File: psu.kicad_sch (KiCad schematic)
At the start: 70 parts, among them J6 Screw_Terminal_01x02, J7 Screw_Terminal_01x03, U12 ADP7182AUJZ, U13 ADP7182AUJZ, U14 AZ1117-ADJ, U15 AZ1117-ADJ, U16 AZ1117-ADJ

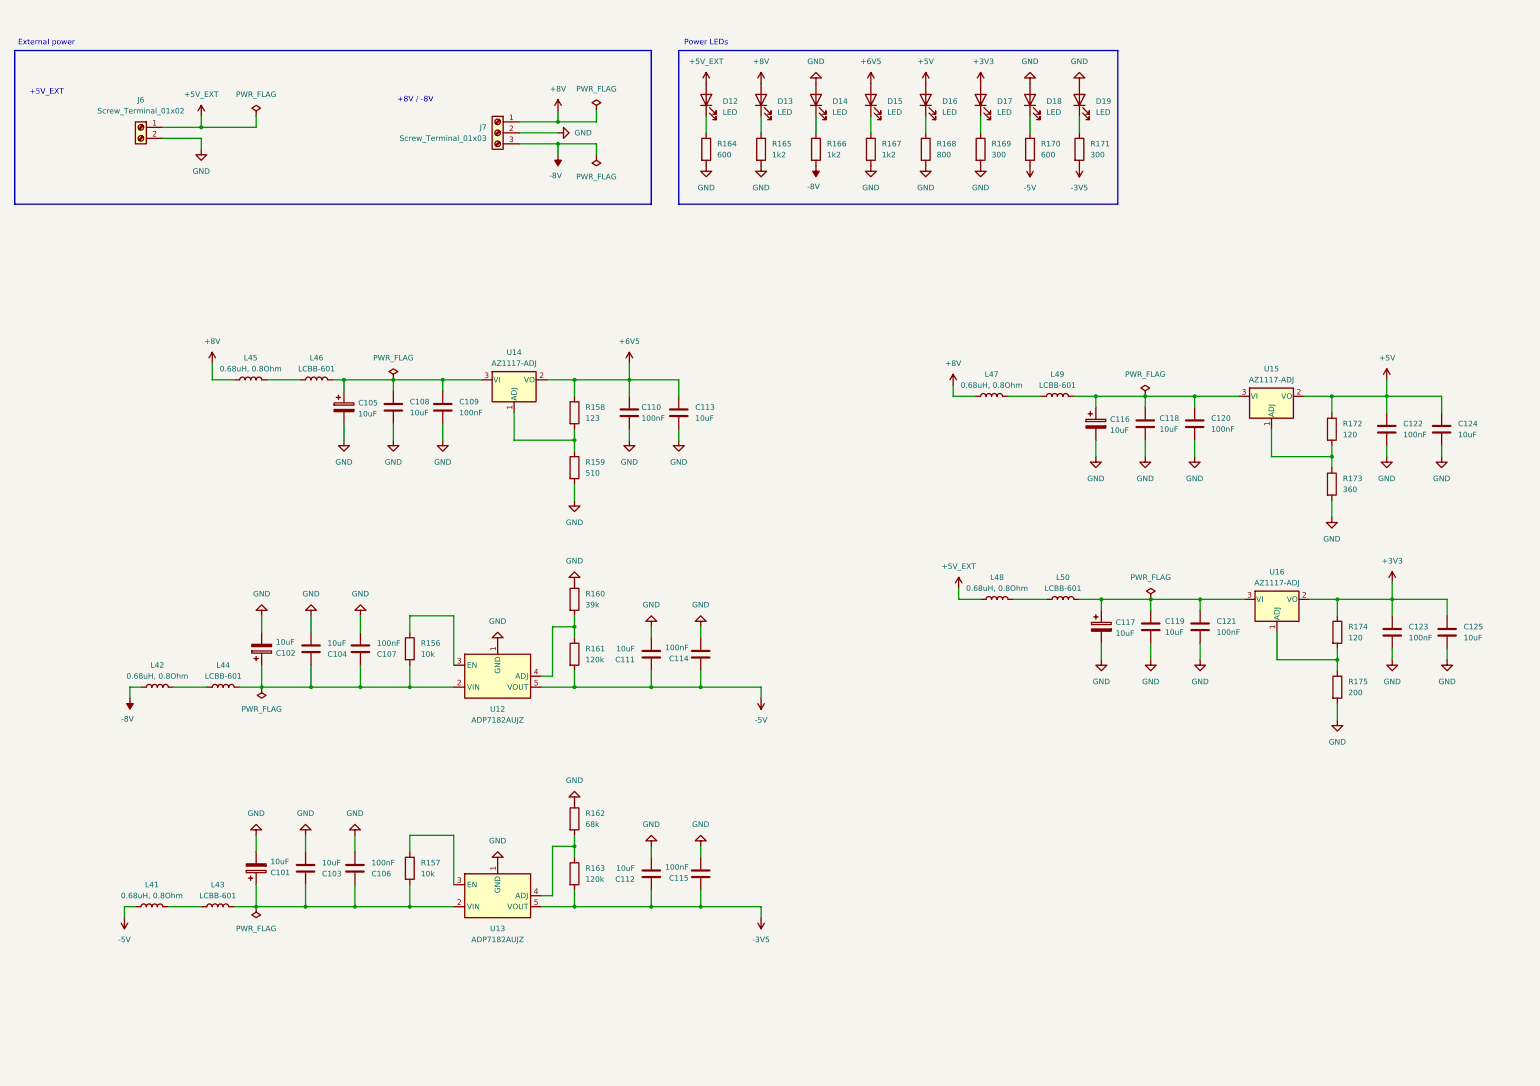
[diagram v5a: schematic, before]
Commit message: Apply changes after review, left to fix: comparator histeresis, PSU missing lines?
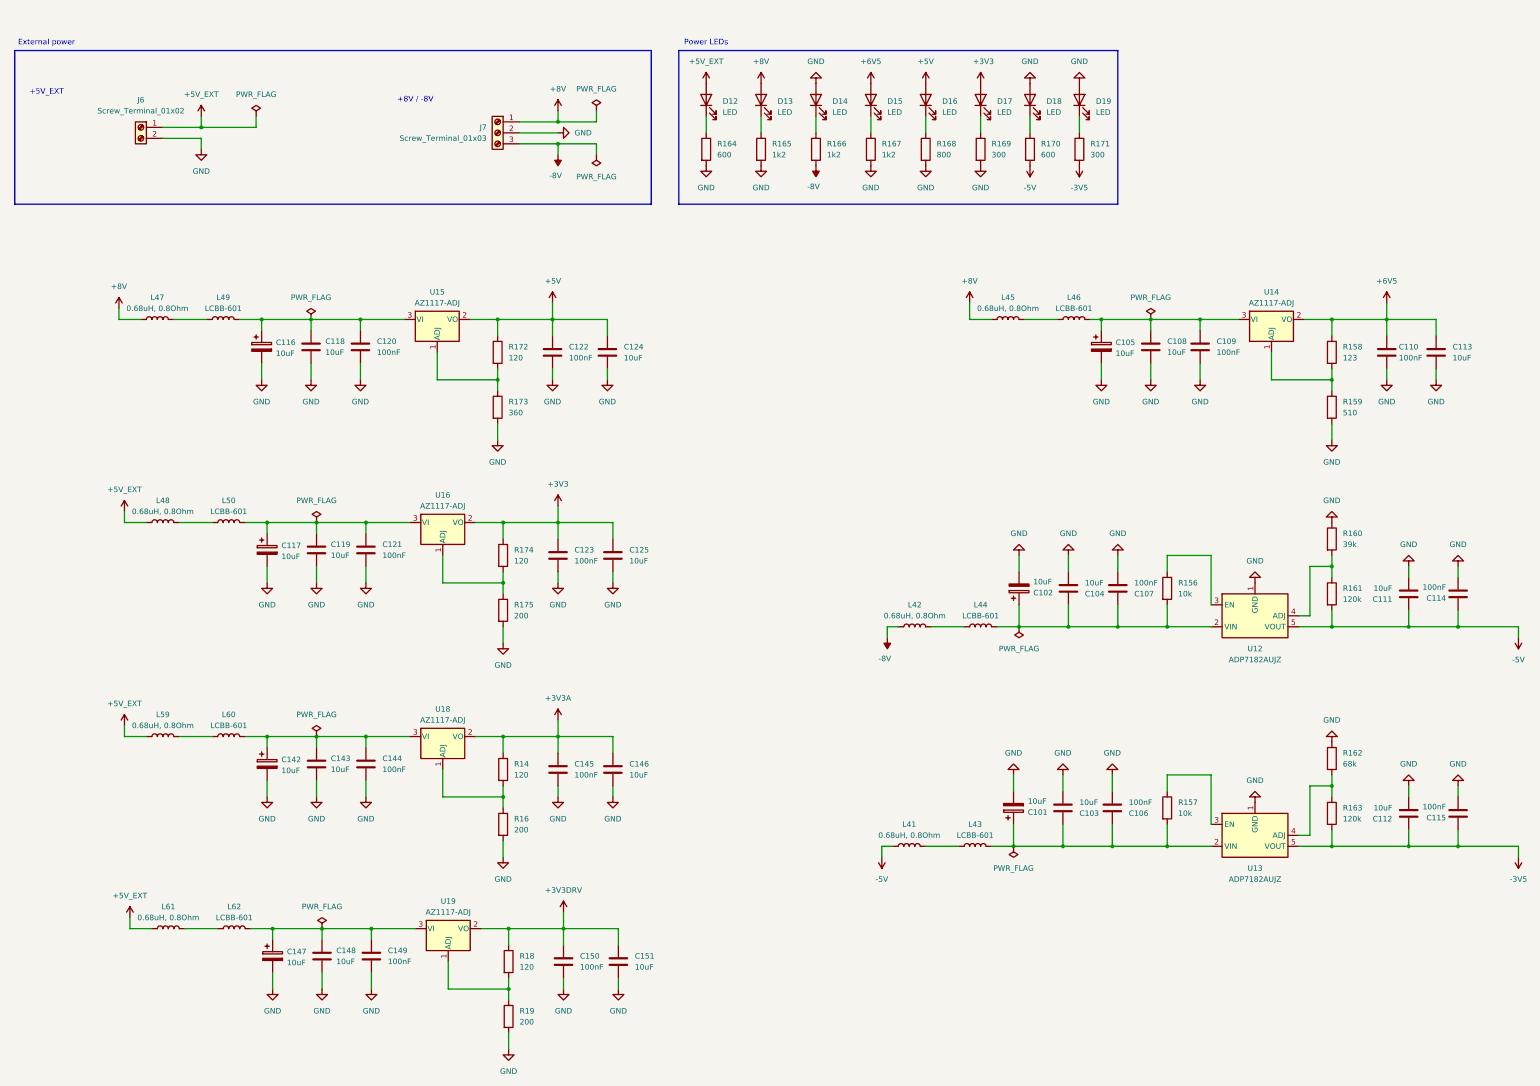
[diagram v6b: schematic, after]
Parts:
- added C142, C147: 10uF, Capacitor_SMD:C_0805_2012Metric, symbol Device:C_Polarized
- added C143, C146, C148, C151: 10uF, Capacitor_SMD:C_0805_2012Metric, symbol Device:C
- added C144, C145, C149, C150: 100nF, Capacitor_SMD:C_0805_2012Metric, symbol Device:C
- added L59, L61: 0.68uH, 0.8Ohm, Inductor_SMD:L_0805_2012Metric, symbol Device:L
- added L60, L62: LCBB-601, Inductor_SMD:L_0805_2012Metric, symbol Device:L
- added R14, R18: 120, Resistor_SMD:R_0805_2012Metric, symbol Device:R
- added R16, R19: 200, Resistor_SMD:R_0805_2012Metric, symbol Device:R
- added U18, U19: AZ1117-ADJ, Package_TO_SOT_SMD:SOT-89-3, symbol Regulator_Linear:AZ1117-ADJ
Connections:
- net +5V_EXT: now also L59.1, L61.1
- net GND: now also C142.2, C143.2, C144.2, C145.2, C146.2, C147.2, C148.2, C149.2, C150.2, C151.2, R16.2, R19.2
- new net: L61.2, L62.1
- new net: C147.1, C148.1, C149.1, L62.2, U19.3 (VI)
- new net: L59.2, L60.1
- new net: R18.2, R19.1, U19.1 (ADJ)
- new net: R14.2, R16.1, U18.1 (ADJ)
- new net: C142.1, C143.1, C144.1, L60.2, U18.3 (VI)
- new net +3V3A: C145.1, C146.1, R14.1, U18.2 (VO)
- new net +3V3DRV: C150.1, C151.1, R18.1, U19.2 (VO)
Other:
- moved on the sheet: C101, C102, C103, C104, C105, C106, C107, C108, C109, C110, C111, C112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

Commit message: Fix footprints and allign components placements
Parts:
- D12, D13, D14: footprint Diode_THT:D_DO-41_SOD81_P10.16mm_Horizontal -> LED_SMD:LED_0805_2012Metric
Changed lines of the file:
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@@
 			)
 		)
-		(property "Footprint" "Diode_THT:D_DO-41_SOD81_P10.16mm_Horizontal"
+		(property "Footprint" "LED_SMD:LED_0805_2012Metric"
 			(at 180.34 36.83 0)
 			(effects
@@
 			)
 		)
-		(property "Footprint" "Diode_THT:D_DO-41_SOD81_P10.16mm_Horizontal"
+		(property "Footprint" "LED_SMD:LED_0805_2012Metric"
 			(at 205.74 36.83 0)
 			(effects
@@
 			)
 		)
-		(property "Footprint" "Diode_THT:D_DO-41_SOD81_P10.16mm_Horizontal"
+		(property "Footprint" "LED_SMD:LED_0805_2012Metric"
 			(at 193.04 36.83 0)
 			(effects

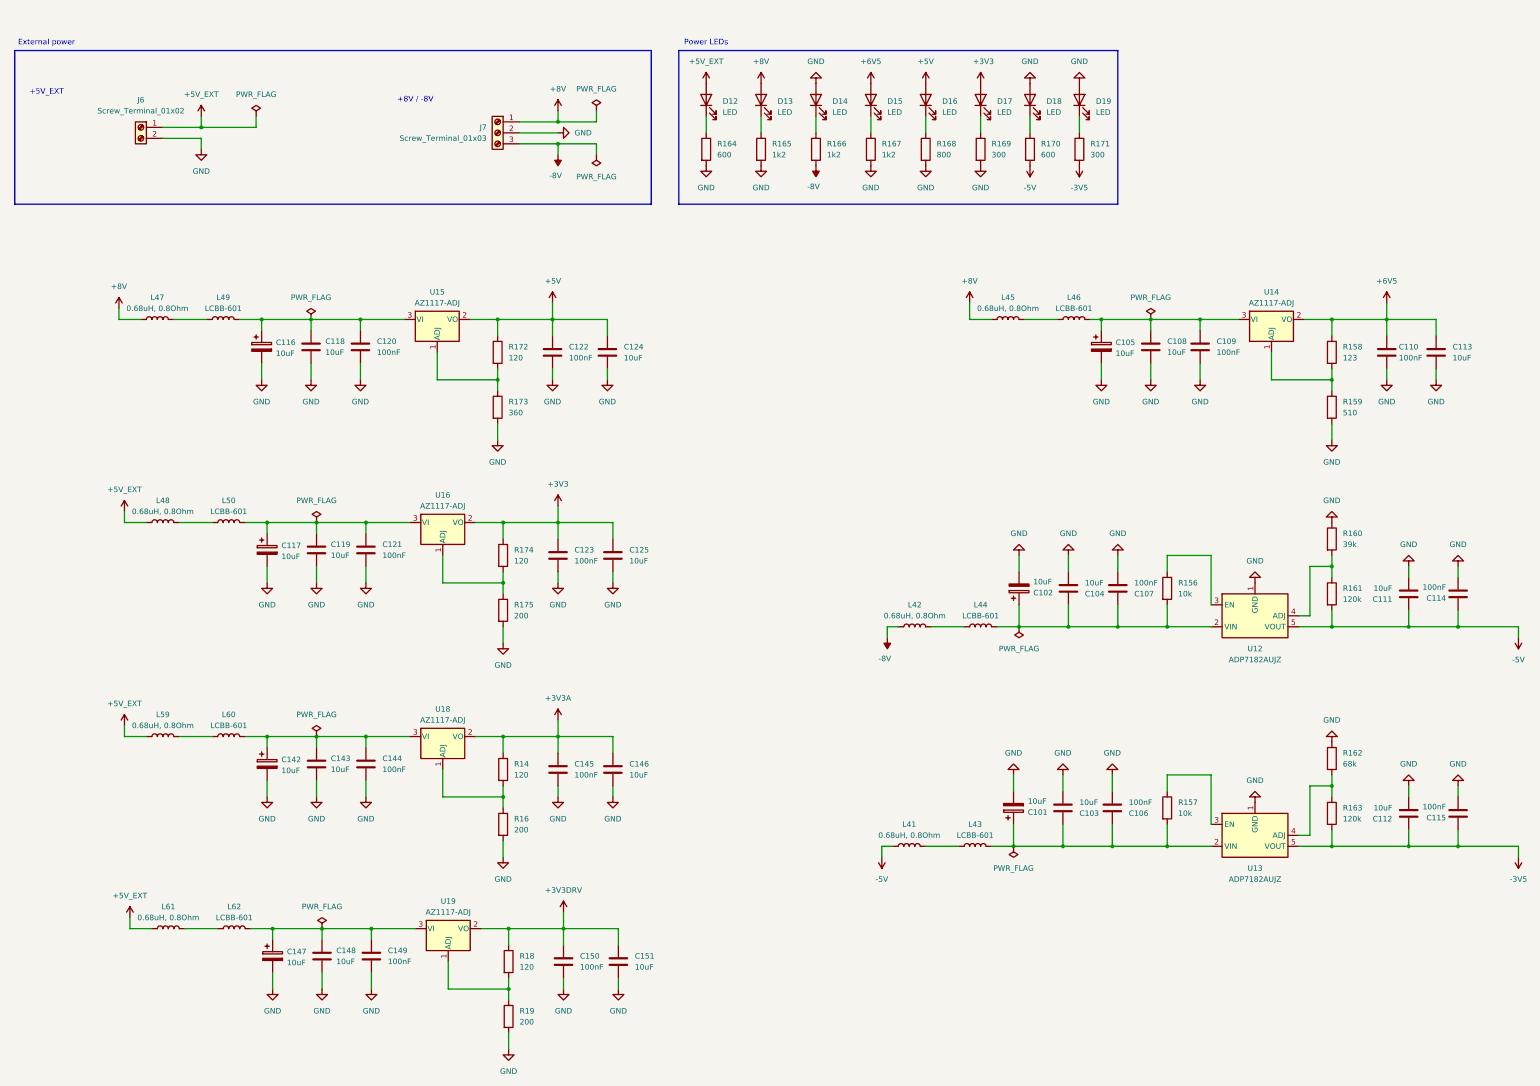
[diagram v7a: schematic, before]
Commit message: Route AFE - attenuators
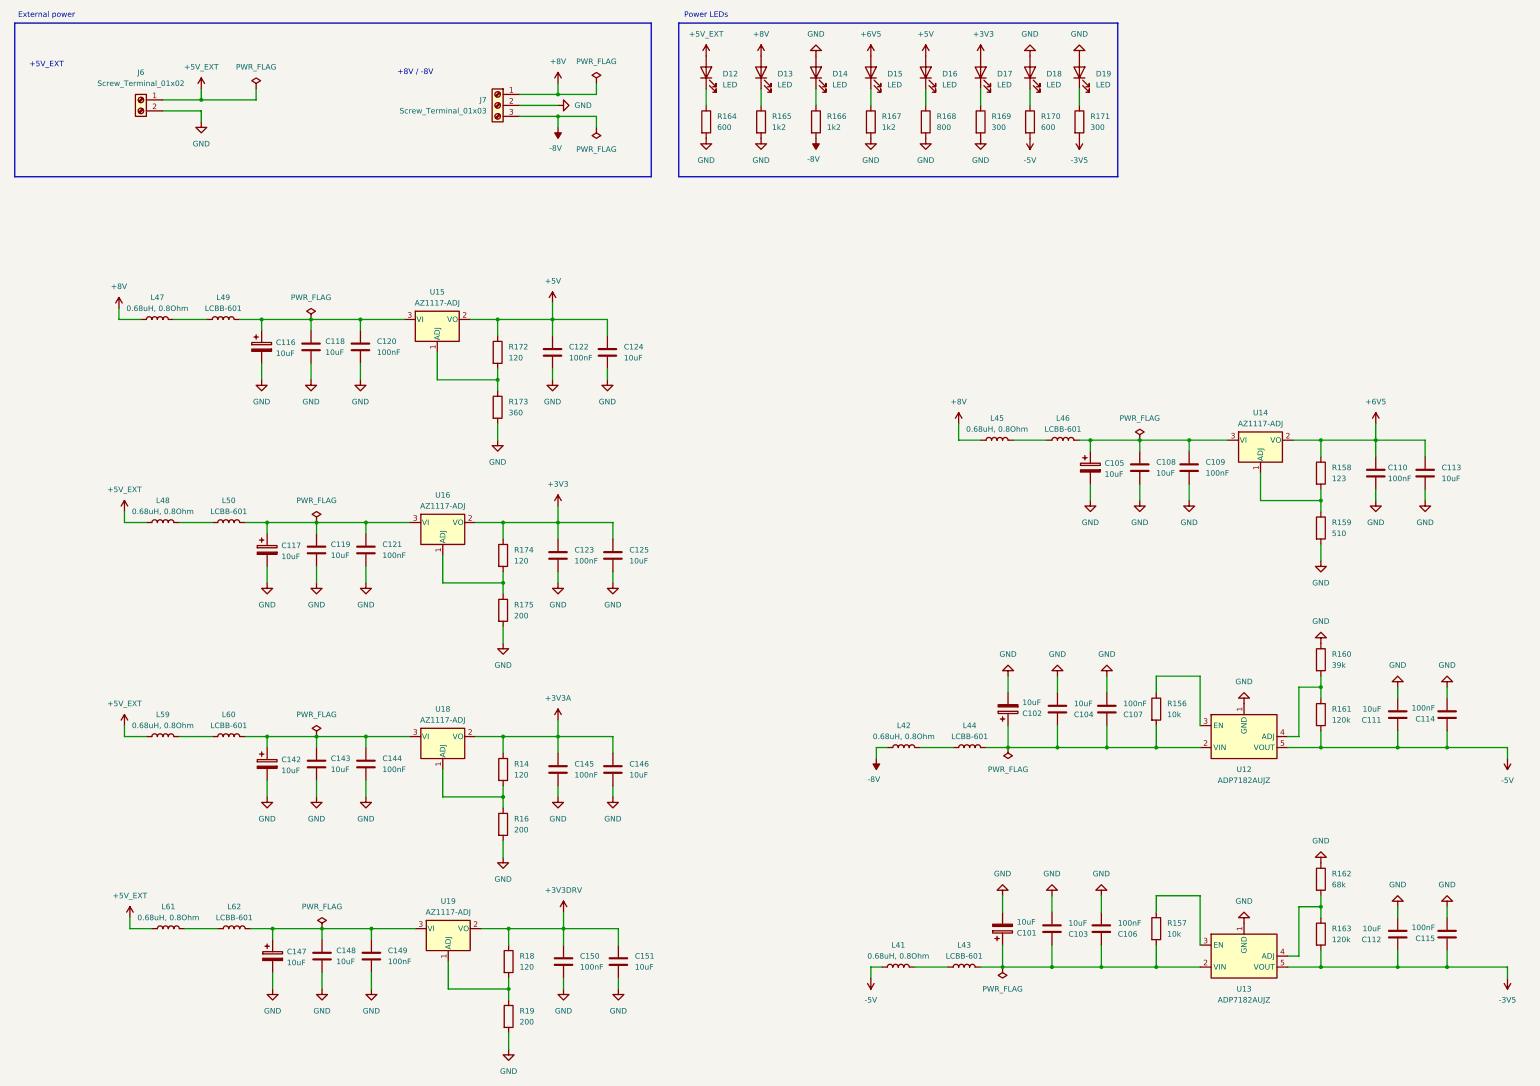
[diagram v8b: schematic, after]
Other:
- moved on the sheet: C101, C102, C103, C104, C105, C106, C107, C108, C109, C110, C111, C112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
